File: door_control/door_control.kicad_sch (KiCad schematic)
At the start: 1 part

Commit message: door control wip
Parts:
- added BZ?: Buzzer, symbol Device:Buzzer
- added C? (x5): 0.1uF, symbol Device:C_Small
- added C? (x3): C_Small, symbol Device:C_Small
- added D? (x5): WS2812B, LED_SMD:LED_WS2812B_PLCC4_5.0x5.0mm_P3.2mm, symbol LED:WS2812B
- added Q?: BSS138, Package_TO_SOT_SMD:SOT-23, symbol Transistor_FET:BSS138
- added R? (x2): 10k, symbol Device:R_Small
- added R?: R_Small, symbol Device:R_Small
- added SW?: 5-Direction_Nav_Switch, door_control_fp:5-Direction_Nav_Switch_THT, symbol door_control:5-Direction_Nav_Switch
- added SW? (x2): SW_Push, symbol Switch:SW_Push
- added U?: LM1117-3.3, symbol Regulator_Linear:LM1117-3.3
- added U?: ESP32-WROOM-32D, RF_Module:ESP32-WROOM-32, symbol RF_Module:ESP32-WROOM-32D
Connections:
- net SD0: now reaches DS?.1 (Data)
- net SD0: now also U?.21 (SDO/SD0)
- net SCLK: now reaches DS?.2 (CLK)
- net SCLK: now also U?.20 (SCK/CLK)
- net RST_OLED: now reaches DS?.4 (Rst)
- net RST_OLED: now also U?.7 (IO35)
- net CS_OLED: now reaches DS?.5 (CS)
- net CS_OLED: now also U?.6 (IO34)
- net +5V: now reaches DS?.7 (Vin)
- net +5V: now also C?.1, C?.1, C?.1, C?.1, C?.1, C?.1, D?.1 (VDD), D?.1 (VDD), D?.1 (VDD), D?.1 (VDD), D?.1 (VDD), R?.2, U?.3 (VI)
- net GND: now reaches DS?.8 (GND)
- net GND: now also C?.2, C?.2, C?.2, C?.2, C?.2, C?.2, C?.2, C?.2, D?.3 (VSS), D?.3 (VSS), D?.3 (VSS), D?.3 (VSS), D?.3 (VSS), SW?.2, SW?.2, SW?.4 (Common), U?.1 (GND), U?.1 (GND), U?.15 (GND), U?.38 (GND), U?.39 (GND)
- new net: D?.2 (DOUT), D?.4 (DIN) (x4)
- new net: D?.4 (DIN), R?.2
- new net: Q?.3 (D), R?.1, R?.1
- new net +3V3: C?.1, C?.1, Q?.1 (G), R?.2, U?.2 (VDD), U?.2 (VO)
- new net button_A: SW?.1
- new net button_B: SW?.1
- new net pixel_DIN: Q?.2 (S), R?.1
- new net sw_center: SW?.6 (Center)
- new net sw_down: SW?.3 (C)
- new net sw_left: SW?.2 (B)
- new net sw_right: SW?.5 (D)
- new net sw_up: SW?.1 (A)
- no-connect marks 0 -> 1
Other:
- note added: "3Vo is 3.3V output from OLED board"
- note added: "Connections to underboard"
- note added: "Level shift"
- note added: "Other Input"
- note added: "Sparkling Button"

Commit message: door control decisions
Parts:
- BZ?: footprint (none) -> Buzzer_Beeper:MagneticBuzzer_Kingstate_KCG0601
- SW?: footprint (none) -> door_control_fp:big_button
- SW?: footprint (none) -> Button_Switch_SMD:SW_Push_1P1T_NO_6x6mm_H9.5mm
- U?: footprint (none) -> Package_TO_SOT_SMD:SOT-223-3_TabPin2
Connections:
- net button_A is gone; now on net main_button: SW?.1
- net button_B is gone; now on net reset_button: SW?.1
- net +5V: now also BZ?.1 (-)
- net sw_center: now also U?.12 (IO27)
- net sw_down: now also U?.10 (IO25)
- net sw_left: now also U?.37 (IO23)
- net sw_right: now also U?.11 (IO26)
- net sw_up: now also U?.36 (IO22)
- net bz_control: now reaches BZ?.2 (+)
- net main_button: now reaches U?.27 (IO16)
- net reset_button: now reaches U?.28 (IO17)
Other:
- note added: "currently randomly chosen :p"
- note added: "need programming header for esp32"
- note added: "reset (hidden) button"
- moved on the sheet: BZ?, DS?

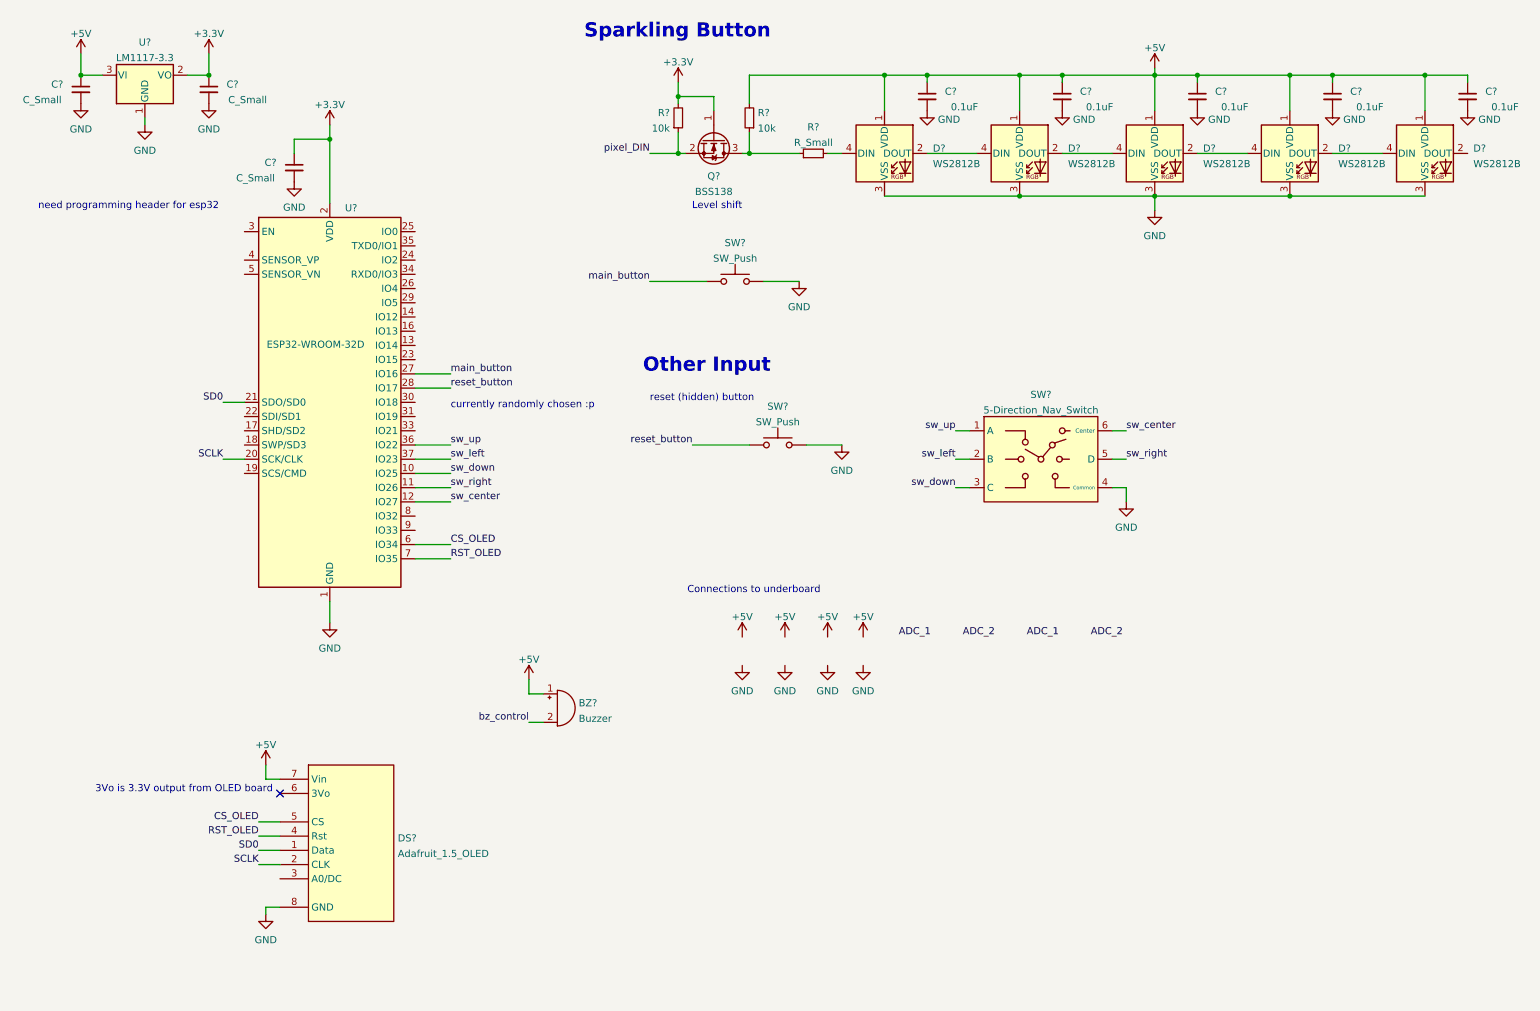
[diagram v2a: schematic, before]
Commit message: Added prog header and underside conn
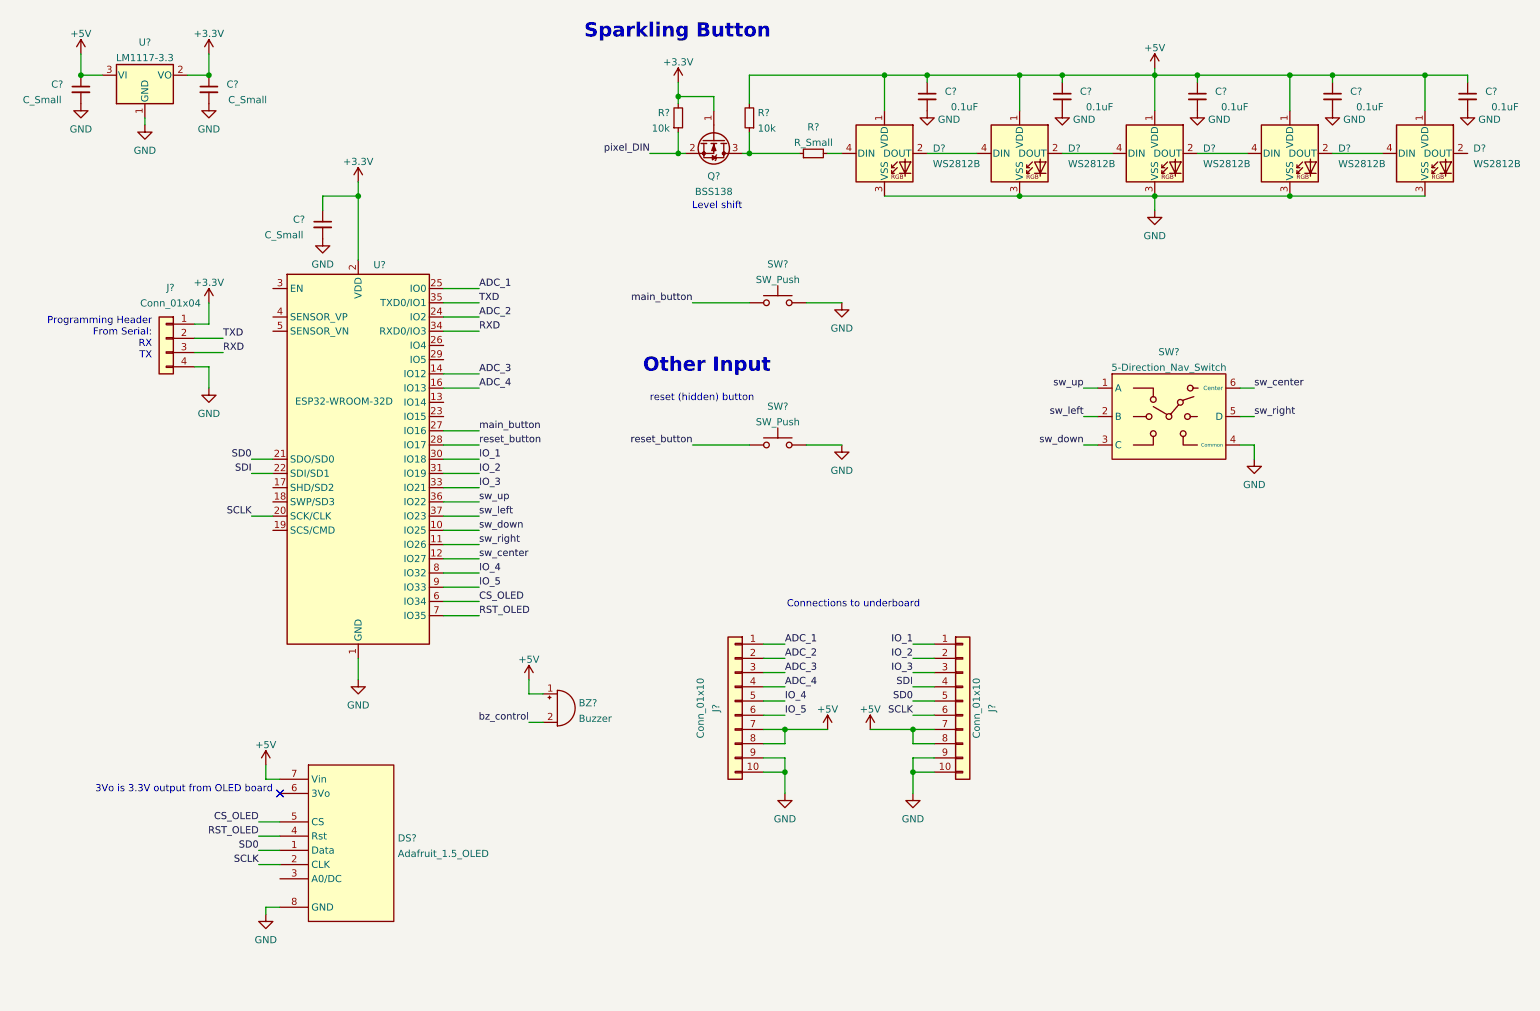
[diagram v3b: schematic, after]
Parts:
- added J?: Conn_01x04, symbol Connector_Generic:Conn_01x04
- added J? (x2): Conn_01x10, symbol Connector_Generic:Conn_01x10
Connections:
- net +3V3: now also J?.1 (Pin_1)
- net +5V: now also J?.7 (Pin_7), J?.7 (Pin_7), J?.8 (Pin_8), J?.8 (Pin_8)
- net ADC_1: now also U?.25 (IO0), J?.1 (Pin_1)
- net ADC_2: now also U?.24 (IO2), J?.2 (Pin_2)
- net GND: now also J?.10 (Pin_10), J?.10 (Pin_10), J?.4 (Pin_4), J?.9 (Pin_9), J?.9 (Pin_9)
- net SCLK: now also J?.6 (Pin_6)
- net SD0: now also J?.5 (Pin_5)
- net ADC_3: now reaches U?.14 (IO12)
- net ADC_3: now also J?.3 (Pin_3)
- net ADC_4: now reaches U?.16 (IO13)
- net ADC_4: now also J?.4 (Pin_4)
- net SDI: now reaches U?.22 (SDI/SD1)
- net SDI: now also J?.4 (Pin_4)
- net IO_1: now reaches U?.30 (IO18)
- net IO_1: now also J?.1 (Pin_1)
- net IO_2: now reaches U?.31 (IO19)
- net IO_2: now also J?.2 (Pin_2)
- net IO_3: now reaches U?.33 (IO21)
- net IO_3: now also J?.3 (Pin_3)
- net RXD: now reaches U?.34 (RXD0/IO3)
- net RXD: now also J?.3 (Pin_3)
- net TXD: now reaches U?.35 (TXD0/IO1)
- net TXD: now also J?.2 (Pin_2)
- net IO_4: now reaches U?.8 (IO32)
- net IO_4: now also J?.5 (Pin_5)
- net IO_5: now reaches U?.9 (IO33)
- net IO_5: now also J?.6 (Pin_6)
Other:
- note added: "Programming Header From Serial: RX TX"
- note removed: "currently randomly chosen :p"
- note removed: "need programming header for esp32"
- moved on the sheet: C?, SW?, U?

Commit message: door control schematic update
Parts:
- added C2, C6, C7: 0.1uF, symbol Device:C_Small
- added C3: 22uF, symbol Device:C_Small
- added R1: 10k, symbol Device:R_Small
- C1, C4: renamed from C?; value C_Small -> 22uF
- C5: renamed from C?; value C_Small -> 0.1uF
- R4: renamed from R?; value R_Small -> 470
- gave numbers to parts that had none: 23
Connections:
- net +3V3: now also BZ1.1 (-), C3.1, R1.2
- net +5V: no longer BZ1.1 (-)
- net GND: now also C2.2, C3.2, C6.2, C7.2
- net SCLK: no longer J3.6 (Pin_6), U2.20 (SCK/CLK)
- net SD0: no longer J3.5 (Pin_5), U2.21 (SDO/SD0)
- net main_button: now also C6.1
- net sw_center: now also U2.9 (IO33); no longer U2.12 (IO27)
- net sw_down: now also U2.12 (IO27); no longer U2.10 (IO25)
- net sw_left: now also U2.11 (IO26); no longer U2.37 (IO23)
- net sw_right: now also U2.8 (IO32); no longer U2.11 (IO26)
- net sw_up: now also U2.10 (IO25); no longer U2.36 (IO22)
- net IO14: now reaches U2.13 (IO14)
- net IO14: now also J3.2 (Pin_2)
- net IO15: now reaches U2.23 (IO15)
- net IO15: now also J3.3 (Pin_3)
- net IO5: now reaches U2.29 (IO5)
- net IO5: now also J3.1 (Pin_1)
- net en: now reaches U2.3 (EN)
- net en: now also SW2.1, C2.1, C7.1, R1.1
- net CS_OLED: no longer names the net of U2.6 (IO34)
- net CS_OLED: no longer DS1.5 (CS)
- net IO_1 renamed IO18
- net IO18: now also J2.5 (Pin_5); no longer J3.1 (Pin_1)
- net IO_2 renamed IO19
- net IO19: now also J2.6 (Pin_6); no longer J3.2 (Pin_2)
- net IO_3: no longer names the net of U2.33 (IO21)
- net IO_3: no longer J3.3 (Pin_3)
- removed net IO_4: J2.5 (Pin_5), U2.8 (IO32)
- removed net IO_5: J2.6 (Pin_6), U2.9 (IO33)
- net SDI renamed IO23
- net IO23: now also U2.37 (IO23); no longer U2.22 (SDI/SD1)
- net reset_button: no longer names the net of U2.28 (IO17)
- net reset_button: no longer SW2.1
- new net SCL: J3.6 (Pin_6), U2.22 (SDI/SD1)
- new net SDA: J3.5 (Pin_5), U2.21 (SDO/SD0)
- no-connect marks 1 -> 8
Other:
- note added: "CS VSPI"
- note added: "Connectors"
- note added: "MISO VSPI"
- note added: "MOSI VSPI"
- note added: "Microcontroller"
- note added: "OLED Screen"
- note added: "Other I/O"
- note added: "SCLK VSPI"
- note added: "Voltage Conversion"
- note removed: "Other Input"
- moved on the sheet: BZ1, C1, C10, C11, C12, C4, C5, C8, C9, D1, D2, D3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
